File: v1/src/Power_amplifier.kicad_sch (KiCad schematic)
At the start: 42 parts, among them U18 TPA3132D2RHBR

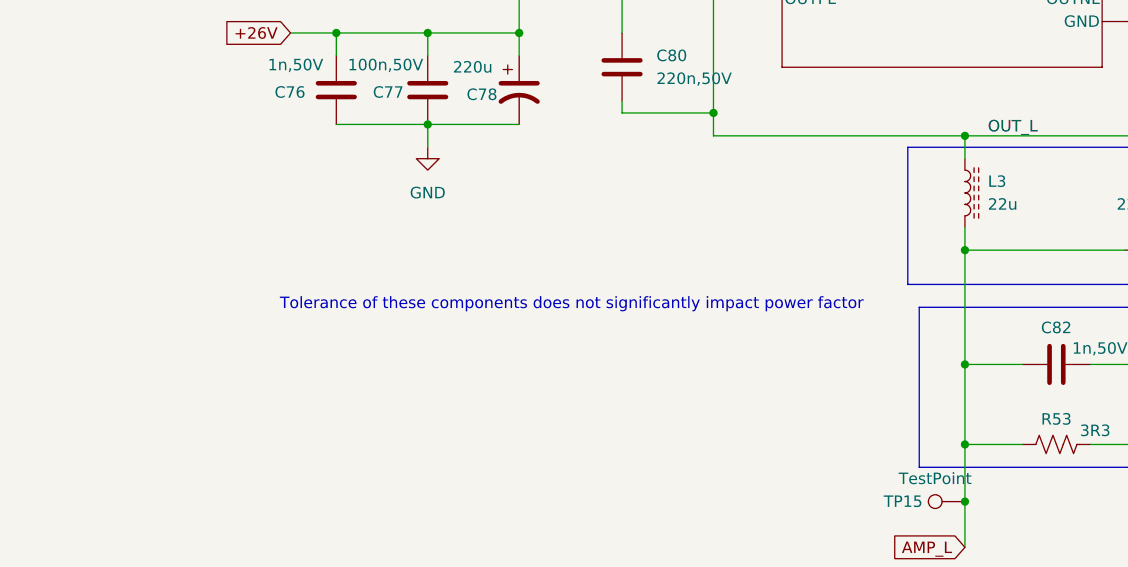
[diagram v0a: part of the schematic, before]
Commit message: Most v2 changes made
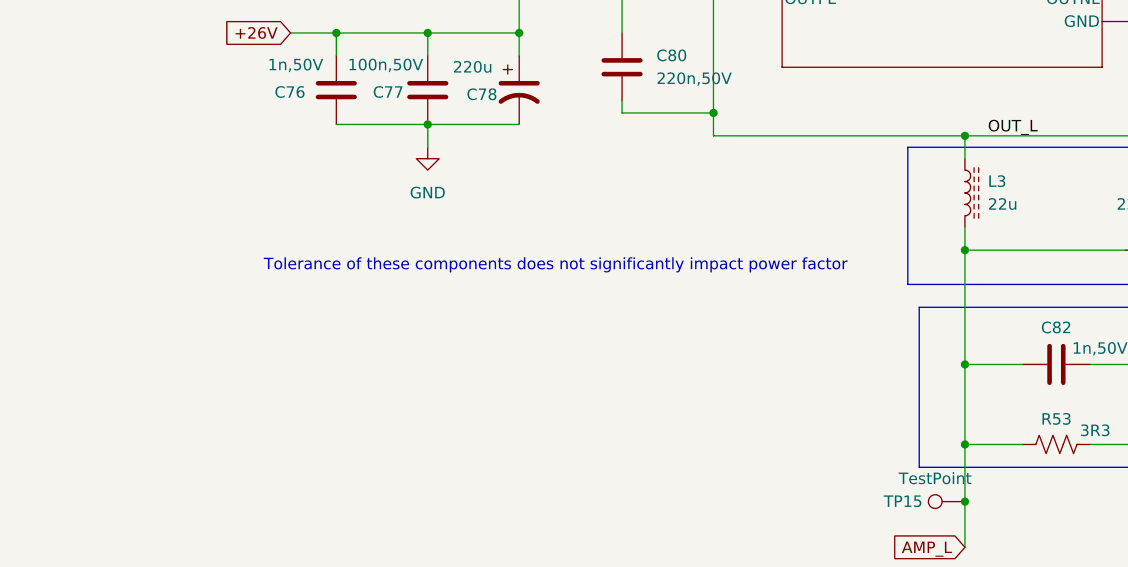
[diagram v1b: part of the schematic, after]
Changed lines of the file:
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@@
 	(text "Tolerance of these components does not significantly impact power factor"
 		(exclude_from_sim no)
-		(at 90.932 136.906 0)
+		(at 89.154 132.588 0)
 		(effects
 			(font
